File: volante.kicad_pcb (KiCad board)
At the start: 2 copper layers, 34 parts, among them J1 ATX-24, J2 Conn_01x02_Pin, J3 Conn_01x02_Pin, Q1 BC817, Q10 BC817, Q11 BC817, Q12 NMOS, Q13 BC817, Q14 BC807, Q15 BC817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

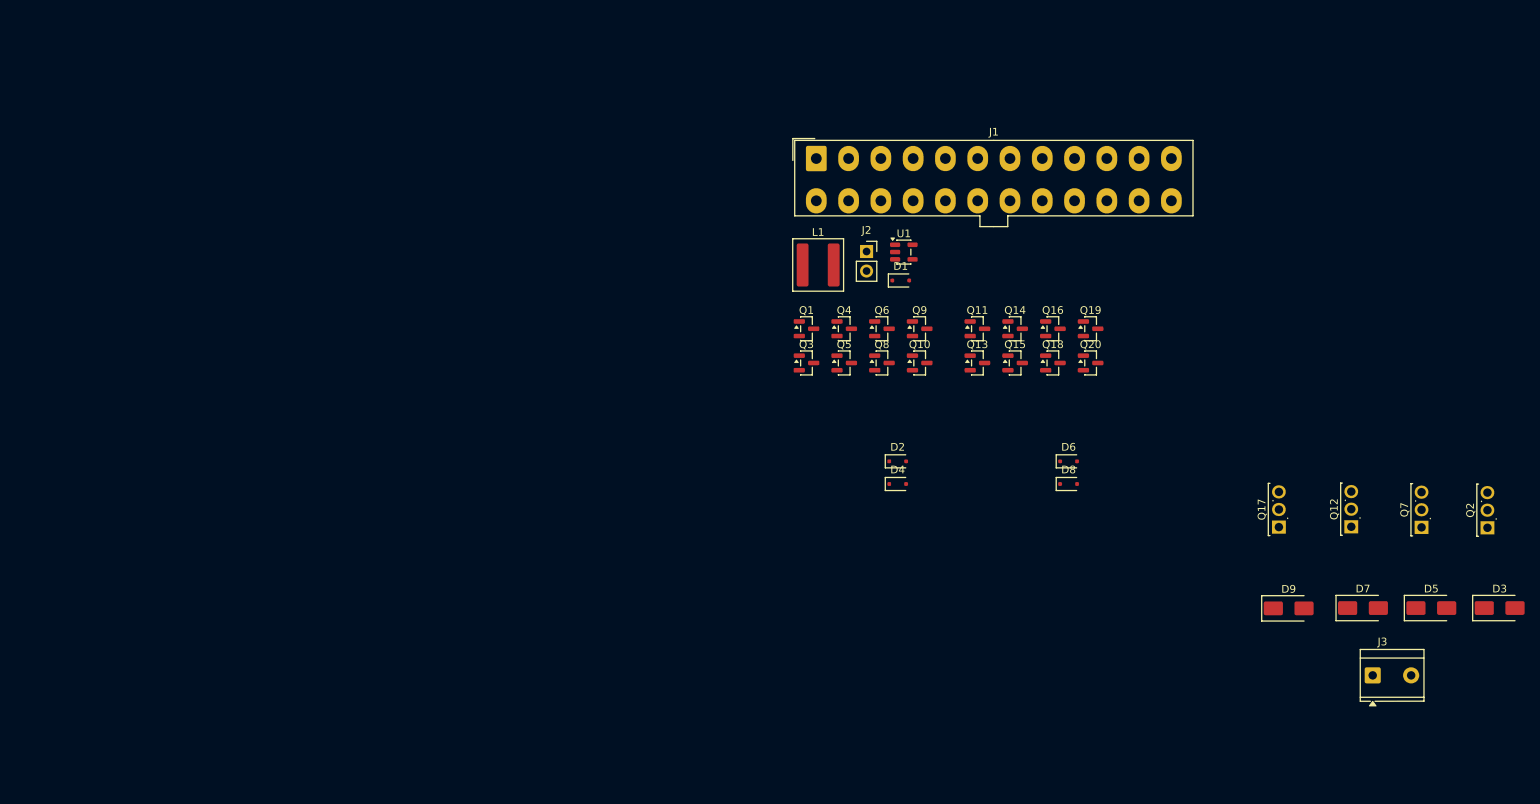
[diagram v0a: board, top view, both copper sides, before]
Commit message: foi adicionado o arduino e conector de encoder na mesma placa, utilizando optacopladores recomeço do layout pcb
 Changes to be committed:
	new file:   controle.kicad_sch
	modified:   dc_converter_sch.kicad_sch
	modified:   half_bridge.kicad_sch
	modified:   volante.kicad_pcb
	modified:   volante.kicad_prl
	modified:   volante.kicad_pro
	modified:   volante.kicad_sch
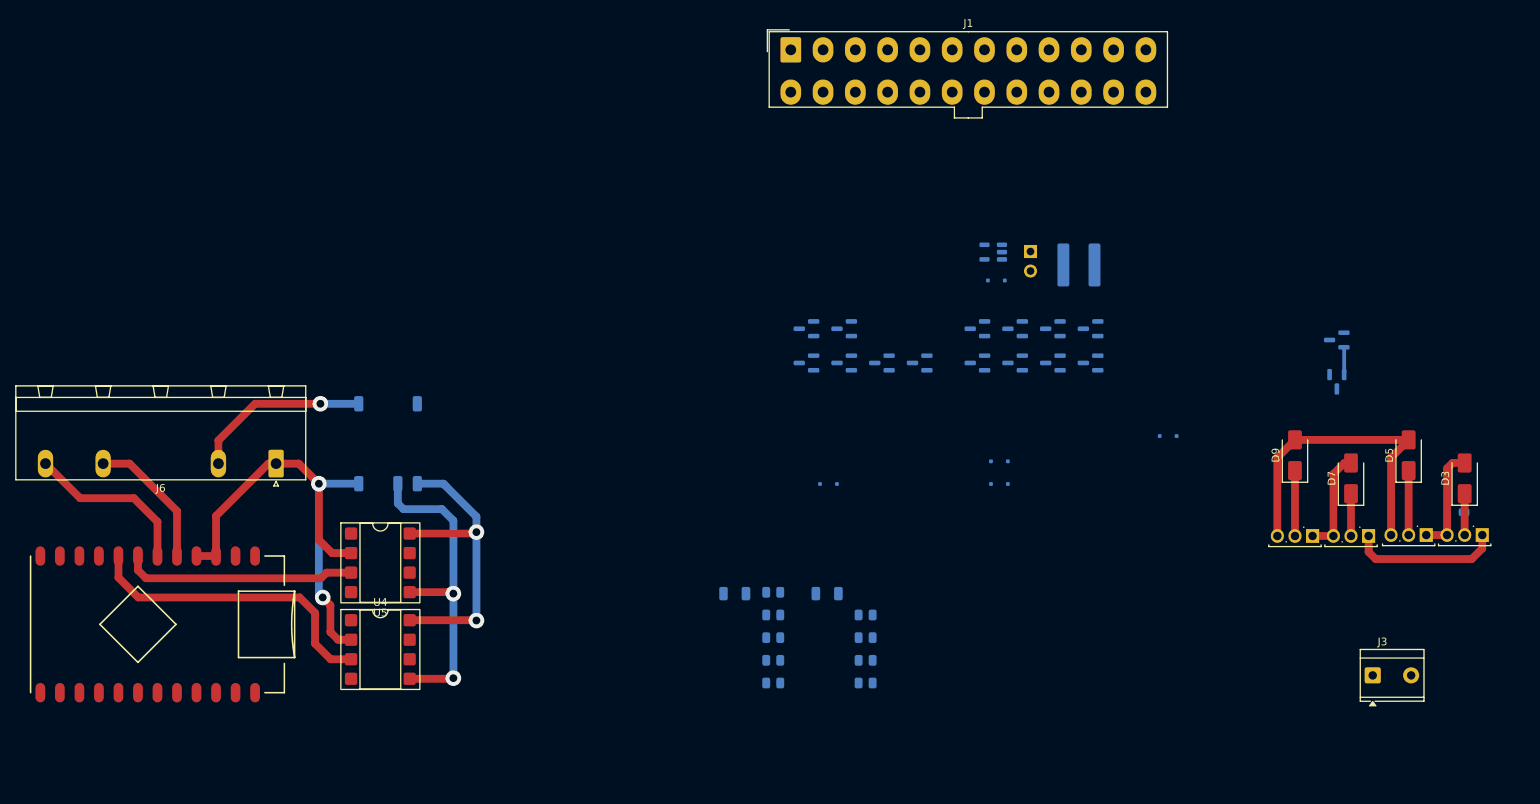
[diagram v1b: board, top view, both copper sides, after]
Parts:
- added J6: Conn_01x04, SUCATA:conector 4 vias 5 espaços verde, F.Cu at (118.9, 100.6)
- added R10: 10K, PCM_SparkFun-Resistor:R_0805_2012Metric, B.Cu at (195.6, 129.1)
- added R12: 33R, PCM_SparkFun-Resistor:R_0805_2012Metric, B.Cu at (183.6, 117.3)
- added R13: 1K, PCM_SparkFun-Resistor:R_1206_3216Metric, B.Cu at (178.6, 117.5)
- added R14: 10K, PCM_SparkFun-Resistor:R_0805_2012Metric, B.Cu at (183.6, 120.3)
- added R16: 33R, PCM_SparkFun-Resistor:R_0805_2012Metric, B.Cu at (183.6, 123.2)
- added R17: 1K, PCM_SparkFun-Resistor:R_0805_2012Metric, B.Cu at (183.6, 126.2)
- added R18: 10K, PCM_SparkFun-Resistor:R_0805_2012Metric, B.Cu at (183.6, 129.1)
- added R4: 33R, PCM_SparkFun-Resistor:R_0805_2012Metric, B.Cu at (273.5, 106.0)
- added R5: 1K, PCM_SparkFun-Resistor:R_1206_3216Metric, B.Cu at (190.6, 117.5)
- added R6: 10K, PCM_SparkFun-Resistor:R_0805_2012Metric, B.Cu at (195.6, 120.3)
- added R8: 33R, PCM_SparkFun-Resistor:R_0805_2012Metric, B.Cu at (195.6, 123.2)
- added R9: 1K, PCM_SparkFun-Resistor:R_0805_2012Metric, B.Cu at (195.6, 126.2)
- added U2: ProMicroC, PCM_SparkFun-Board:ProMicroC, F.Cu at (103.5, 121.5)
- added U3: ~, Converter_DCDC:Converter_DCDC_TRACO_TES1-051x_121x_241x_Single_SMD, B.Cu at (133.5, 98.0)
- added U4: 6N137, Package_DIP:DIP-8_W7.62mm_SMDSocket_SmallPads, F.Cu at (132.5, 124.8)
- added U5: 6N137, Package_DIP:DIP-8_W7.62mm_SMDSocket_SmallPads, F.Cu at (132.5, 113.5)
- D1, D2, D4, D6, D8, J2, L1, Q1, Q10, Q11, Q13, Q14, Q15, Q16, Q18, Q19, Q20, Q3, Q4, Q5, Q6, Q8, Q9, U1: moved to B.Cu
- moved Q11 46.8 mm to (256.9, 84.5), turned to 180 degrees
- moved Q14 42.4 mm to (256.9, 89.9), turned to -90 degrees
- moved Q1 37.0 mm to (224.9, 83.0), turned to 180 degrees
- moved Q19 37.0 mm to (187.9, 83.0), turned to 180 degrees
- moved Q20 37.0 mm to (187.9, 87.5), turned to 180 degrees
- moved Q3 37.0 mm to (224.9, 87.5), turned to 180 degrees
- moved L1 33.9 mm to (223.4, 74.7), turned to 180 degrees
- moved D8 31.2 mm to (190.8, 103.2), turned to 180 degrees
- moved Q16 27.2 mm to (192.8, 83.0), turned to 180 degrees
- moved Q18 27.2 mm to (192.8, 87.5), turned to 180 degrees
- moved Q4 27.2 mm to (220.0, 83.0), turned to 180 degrees
- moved Q5 27.2 mm to (220.0, 87.5), turned to 180 degrees
- moved J2 21.3 mm to (217.1, 73.0), turned to 180 degrees
- moved D5 20.1 mm to (266.3, 99.5), turned to 90 degrees
- moved D9 19.9 mm to (251.5, 99.5), turned to 90 degrees
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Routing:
- net GND: track 0.00 -> 82.0 mm, vias 0 -> 2
- net GNG_ISO: track 0.00 -> 65.5 mm, vias 0 -> 2
- net V05: track 0.00 -> 42.7 mm, vias 0 -> 2
- net PWM_CW_ISO: track 0.00 -> 39.8 mm
- net PWM_CC_ISO: track 0.00 -> 30.3 mm
- net V12_ISO: track 0.00 -> 23.3 mm, vias 0 -> 1
- net Net-(J6-Pin_4): track 0.00 -> 22.2 mm
- net V12: track 0.00 -> 19.6 mm
- net Net-(J6-Pin_3): track 0.00 -> 18.0 mm
- net /Ponte H/meia ponte B/M: track 0.00 -> 14.0 mm
- net /Ponte H/meia ponte A/M: track 0.00 -> 13.7 mm
- net /Ponte H/meia ponte A/Gl: track 0.00 -> 8.50 mm
- net /Ponte H/meia ponte B/Gh: track 0.00 -> 8.38 mm
- net /Ponte H/meia ponte B/Gl: track 0.00 -> 8.38 mm
- net /Ponte H/meia ponte A/Gh: track 0.00 -> 5.50 mm
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
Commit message: alteração no circuito de controle: adição dos isoladores
  Changes to be committed:
 	new file:   .history
 	modified:   controle.kicad_sch
 	modified:   dc_converter_sch.kicad_sch
 	modified:   h_bridge_sch.kicad_sch
 	modified:   half_bridge.kicad_sch
 	modified:   volante.kicad_pcb
 	modified:   volante.kicad_prl
 	modified:   volante.kicad_pro
 	modified:   volante.kicad_sch

  Changes not staged for commit:
 	modified:   .history (modified content, untracked content)
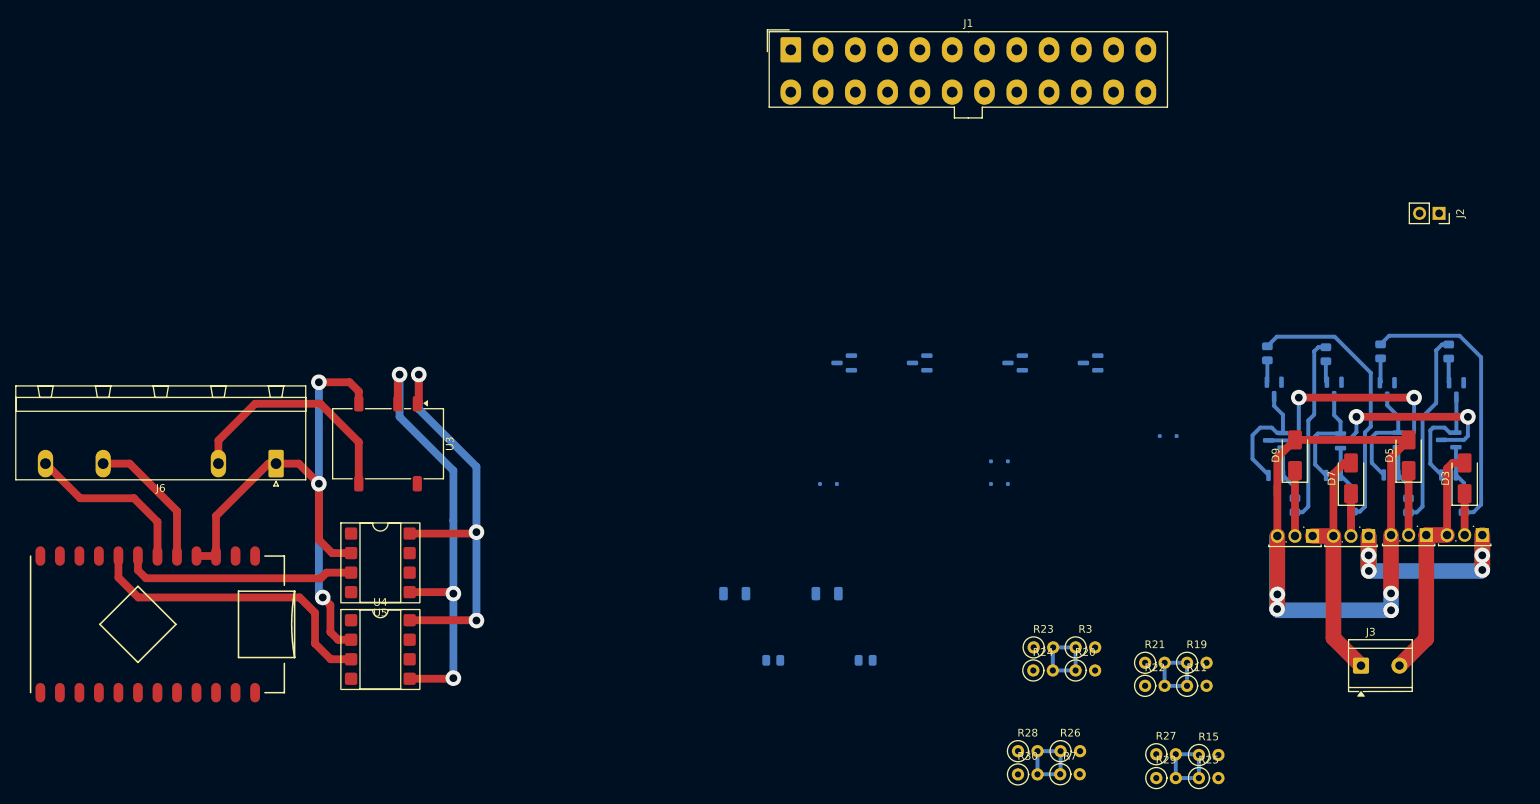
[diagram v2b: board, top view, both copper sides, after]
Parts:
- removed D1: BAS516, Diode_SMD:D_SOD-323F
- removed L1: 15uH, Inductor_SMD:L_Bourns_SRP6060FA
- removed U1: AP3012, Package_TO_SOT_SMD:SOT-23-5
- added R11: 1K, Resistor_THT:R_Axial_DIN0207_L6.3mm_D2.5mm_P2.54mm_Vertical, F.Cu at (237.5, 129.5)
- added R15: 1K, Resistor_THT:R_Axial_DIN0207_L6.3mm_D2.5mm_P2.54mm_Vertical, F.Cu at (239.0, 138.5)
- added R19: 1K, Resistor_THT:R_Axial_DIN0207_L6.3mm_D2.5mm_P2.54mm_Vertical, F.Cu at (237.5, 126.5)
- added R20: 1K, Resistor_THT:R_Axial_DIN0207_L6.3mm_D2.5mm_P2.54mm_Vertical, F.Cu at (223.0, 127.5)
- added R21: 1K, Resistor_THT:R_Axial_DIN0207_L6.3mm_D2.5mm_P2.54mm_Vertical, F.Cu at (232.0, 126.5)
- added R22: 1K, Resistor_THT:R_Axial_DIN0207_L6.3mm_D2.5mm_P2.54mm_Vertical, F.Cu at (232.0, 129.5)
- added R23: 1K, Resistor_THT:R_Axial_DIN0207_L6.3mm_D2.5mm_P2.54mm_Vertical, F.Cu at (217.5, 124.5)
- added R24: 1K, Resistor_THT:R_Axial_DIN0207_L6.3mm_D2.5mm_P2.54mm_Vertical, F.Cu at (217.5, 127.5)
- added R25: 1K, Resistor_THT:R_Axial_DIN0207_L6.3mm_D2.5mm_P2.54mm_Vertical, F.Cu at (239.0, 141.5)
- added R26: 1K, Resistor_THT:R_Axial_DIN0207_L6.3mm_D2.5mm_P2.54mm_Vertical, F.Cu at (221.0, 138.0)
- added R27: 1K, Resistor_THT:R_Axial_DIN0207_L6.3mm_D2.5mm_P2.54mm_Vertical, F.Cu at (233.5, 138.4)
- added R28: 1K, Resistor_THT:R_Axial_DIN0207_L6.3mm_D2.5mm_P2.54mm_Vertical, F.Cu at (215.5, 138.0)
- added R29: 1K, Resistor_THT:R_Axial_DIN0207_L6.3mm_D2.5mm_P2.54mm_Vertical, F.Cu at (233.5, 141.5)
- added R3: 1K, Resistor_THT:R_Axial_DIN0207_L6.3mm_D2.5mm_P2.54mm_Vertical, F.Cu at (223.0, 124.5)
- added R30: 1K, Resistor_THT:R_Axial_DIN0207_L6.3mm_D2.5mm_P2.54mm_Vertical, F.Cu at (215.5, 141.0)
- added R7: 1K, Resistor_THT:R_Axial_DIN0207_L6.3mm_D2.5mm_P2.54mm_Vertical, F.Cu at (221.0, 141.0)
- J2, U3: moved to F.Cu
- moved R6 83.2 mm to (271.5, 86.0), turned to -90 degrees
- moved R10 79.7 mm to (262.6, 86.0), turned to -90 degrees
- moved R14 79.5 mm to (255.5, 86.4), turned to -90 degrees
- moved R18 77.3 mm to (247.9, 86.2), turned to -90 degrees
- moved R12 76.2 mm to (259.0, 105.9), turned to -90 degrees
- moved R8 72.7 mm to (266.3, 106.0), turned to -90 degrees
- moved R16 70.0 mm to (251.5, 106.0), turned to -90 degrees
- moved Q19 64.3 mm to (249.0, 103.1), turned to -90 degrees
- moved Q20 61.0 mm to (248.8, 90.9), turned to -90 degrees
- moved Q15 58.9 mm to (256.6, 90.9), turned to -90 degrees
- moved Q16 58.0 mm to (249.0, 97.6)
- moved Q9 57.4 mm to (264.0, 103.0), turned to -90 degrees
- moved Q4 55.2 mm to (271.5, 103.0), turned to -90 degrees
- moved Q10 53.4 mm to (263.5, 91.0), turned to -90 degrees
- moved J2 53.4 mm to (270.2, 68.0), turned to -90 degrees
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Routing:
- net GND: track 82.0 -> 153.9 mm, vias 2 -> 7
- net V12: track 19.6 -> 67.8 mm, vias 0 -> 6
- net /Ponte H/meia ponte A/Gh: track 5.50 -> 44.3 mm
- net /Ponte H/meia ponte B/Gh: track 8.38 -> 44.9 mm
- net /Ponte H/meia ponte B/Gl: track 8.38 -> 36.5 mm
- net /Ponte H/meia ponte A/Gl: track 8.50 -> 35.9 mm
- net V22: track 0.00 -> 27.1 mm, vias 0 -> 2
- net /Ponte H/meia ponte B/M: track 14.0 -> 38.4 mm
- net /Ponte H/meia ponte A/M: track 13.7 -> 38.0 mm
- net Net-(Q16-B): track 0.00 -> 15.8 mm
- net GNG_ISO: track 65.5 -> 80.8 mm, vias 2 -> 3
- net V05: track 42.7 -> 57.8 mm, vias 2 -> 3
- net Net-(Q1-B): track 0.00 -> 14.7 mm
- net Net-(Q10-C): track 0.00 -> 14.4 mm
- net Net-(Q11-B): track 0.00 -> 14.3 mm
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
